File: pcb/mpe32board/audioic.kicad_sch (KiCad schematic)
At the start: 13 parts, among them J47 AudioJack3_Ground, U1 TAC5212IRGER

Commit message: layout stuff
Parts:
- C26, C27, C28, C29, C30, C31, C32, C33, C34: footprint (none) -> Capacitor_SMD:C_0603_1608Metric
- R41, R42: footprint (none) -> Resistor_SMD:R_0603_1608Metric
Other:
- note added: "https://www.ti.com/lit/ug/slau902a/slau902a.pdf (pg 11) https://github.com/t-dsp/t-dsp_tac5212_pro_audio_module/blob/main/documentation/t-dsp-tac5212-schematic.pdf"
- moved on the sheet: J47
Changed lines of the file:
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@@
 	(generator_version "9.0")
 	(paper "A4")
+	(text "https://www.ti.com/lit/ug/slau902a/slau902a.pdf (pg 11)\nhttps://github.com/t-dsp/t-dsp_tac5212_pro_audio_module/blob/main/documentation/t-dsp-tac5212-schematic.pdf"
+		(exclude_from_sim no)
+		(at 176.276 133.604 0)
+		(effects
+			(font
+				(size 1.27 1.27)
+			)
+		)
+	)
 	(junction
 		(at 119.38 57.15)
@@
 	(wire
 		(pts
-			(xy 252.73 60.96) (xy 252.73 59.69)
+			(xy 245.11 52.07) (xy 245.11 50.8)
 		)
 		(stroke
@@
 	(wire
 		(pts
-			(xy 252.73 59.69) (xy 236.22 59.69)
+			(xy 245.11 50.8) (xy 228.6 50.8)
 		)
 		(stroke
@@
 	(global_label "L_CHANNEL"
 		(shape input)
-		(at 236.22 64.77 0)
+		(at 228.6 55.88 0)
 		(fields_autoplaced yes)
 		(effects
@@
 		)
 		(property "Intersheetrefs" "${INTERSHEET_REFS}"
-			(at 249.7281 64.77 0)
+			(at 242.1081 55.88 0)
 			(effects
 				(font
@@
 	(global_label "R_CHANNEL"
 		(shape input)
-		(at 236.22 62.23 0)
+		(at 228.6 53.34 0)
 		(fields_autoplaced yes)
 		(effects
@@
 		)
 		(property "Intersheetrefs" "${INTERSHEET_REFS}"
-			(at 249.97 62.23 0)
+			(at 242.35 53.34 0)
 			(effects
 				(font
@@
 			)
 		)
-		(property "Footprint" ""
+		(property "Footprint" "Capacitor_SMD:C_0603_1608Metric"
 			(at 191.77 58.42 0)
 			(effects
@@
 			)
 		)
-		(property "Footprint" ""
+		(property "Footprint" "Capacitor_SMD:C_0603_1608Metric"
 			(at 167.64 48.26 0)
 			(effects
@@
 	(symbol
 		(lib_id "power:GND")
-		(at 231.14 69.85 0)
+		(at 223.52 60.96 0)
 		(unit 1)
 		(exclude_from_sim no)
@@
 		(fields_autoplaced yes)
 		(property "Reference" "#PWR0150"
-			(at 231.14 76.2 0)
+			(at 223.52 67.31 0)
 			(effects
 				(font
@@
 		)
 		(property "Value" "GND"
-			(at 231.14 74.93 0)
+			(at 223.52 66.04 0)
 			(effects
 				(font
@@
 		)
 		(property "Footprint" ""
-			(at 231.14 69.85 0)
+			(at 223.52 60.96 0)
 			(effects
 				(font
@@
 		)
 		(property "Datasheet" ""
-			(at 231.14 69.85 0)
+			(at 223.52 60.96 0)
 			(effects
 				(font
@@
 		)
 		(property "Description" "Power symbol creates a global label with name \"GND\" , ground"
-			(at 231.14 69.85 0)
+			(at 223.52 60.96 0)
 			(effects
 				(font
@@
 	(symbol
 		(lib_id "Connector_Audio:AudioJack3_Ground")
-		(at 231.14 62.23 0)
+		(at 223.52 53.34 0)
 		(unit 1)
 		(exclude_from_sim no)
@@
 		(fields_autoplaced yes)
 		(property "Reference" "J47"
-			(at 229.235 53.34 0)
+			(at 221.615 44.45 0)
 			(effects
 				(font
@@
 		)
 		(property "Value" "AudioJack3_Ground"
-			(at 229.235 55.88 0)
+			(at 221.615 46.99 0)
 			(effects
 				(font
@@
 		)
 		(property "Footprint" "Connector_Audio:Jack_3.5mm_CUI_SJ-3524-SMT_Horizontal"
-			(at 231.14 62.23 0)
+			(at 223.52 53.34 0)
 			(effects
 				(font
@@
 		)
 		(property "Datasheet" "~"
-			(at 231.14 62.23 0)
+			(at 223.52 53.34 0)
 			(effects
 				(font
@@
 		)
 		(property "Description" "Audio Jack, 3 Poles (Stereo / TRS), Grounded Sleeve"
-			(at 231.14 62.23 0)
+			(at 223.52 53.34 0)
 			(effects
 				(font
@@
 			)
 		)
-		(property "Footprint" ""
+		(property "Footprint" "Capacitor_SMD:C_0603_1608Metric"
 			(at 123.19 46.99 0)
 			(effects
@@
 			)
 		)
-		(property "Footprint" ""
+		(property "Footprint" "Capacitor_SMD:C_0603_1608Metric"
 			(at 143.51 57.15 0)
 			(effects
@@
 			)
 		)
-		(property "Footprint" ""
+		(property "Footprint" "Resistor_SMD:R_0603_1608Metric"
 			(at 93.98 107.95 0)
 			(effects
@@
 			)
 		)
-		(property "Footprint" ""
+		(property "Footprint" "Capacitor_SMD:C_0603_1608Metric"
 			(at 196.85 102.87 0)
 			(effects
@@
 	(symbol
 		(lib_id "power:GND")
-		(at 252.73 60.96 0)
+		(at 245.11 52.07 0)
 		(unit 1)
 		(exclude_from_sim no)
@@
 		(fields_autoplaced yes)
 		(property "Reference" "#PWR0159"
-			(at 252.73 67.31 0)
+			(at 245.11 58.42 0)
 			(effects
 				(font
@@
 		)
 		(property "Value" "GND"
-			(at 252.73 66.04 0)
+			(at 245.11 57.15 0)
 			(effects
 				(font
@@
 		)
 		(property "Footprint" ""
-			(at 252.73 60.96 0)
+			(at 245.11 52.07 0)
 			(effects
 				(font
@@
 		)
 		(property "Datasheet" ""
-			(at 252.73 60.96 0)
+			(at 245.11 52.07 0)
 			(effects
 				(font
@@
 		)
 		(property "Description" "Power symbol creates a global label with name \"GND\" , ground"
-			(at 252.73 60.96 0)
+			(at 245.11 52.07 0)
 			(effects
 				(font
@@
 			)
 		)
-		(property "Footprint" ""
+		(property "Footprint" "Capacitor_SMD:C_0603_1608Metric"
 			(at 167.64 58.42 0)
 			(effects
@@
 			)
 		)
-		(property "Footprint" ""
+		(property "Footprint" "Resistor_SMD:R_0603_1608Metric"
 			(at 93.98 100.33 0)
 			(effects
@@
 			)
 		)
-		(property "Footprint" ""
+		(property "Footprint" "Capacitor_SMD:C_0603_1608Metric"
 			(at 123.19 57.15 0)
 			(effects
@@
 			)
 		)
-		(property "Footprint" ""
+		(property "Footprint" "Capacitor_SMD:C_0603_1608Metric"
 			(at 201.93 100.33 0)
 			(effects
@@
 			)
 		)
-		(property "Footprint" ""
+		(property "Footprint" "Capacitor_SMD:C_0603_1608Metric"
 			(at 191.77 48.26 0)
 			(effects

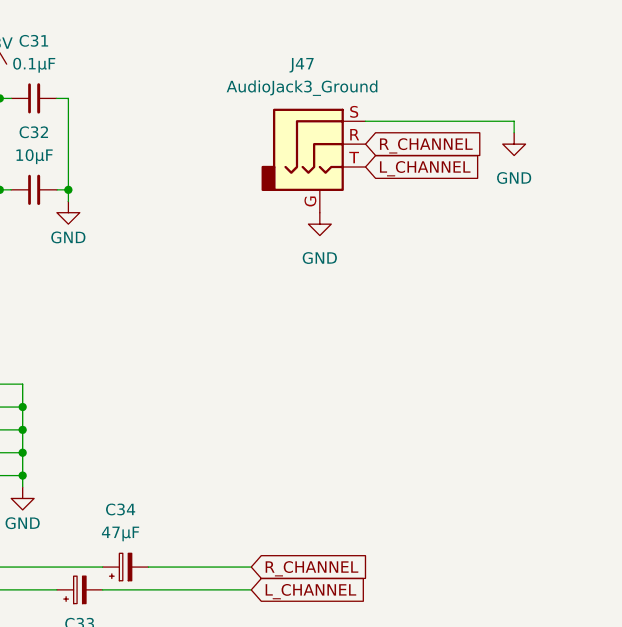
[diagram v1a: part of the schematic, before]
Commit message: routed data bus of ram
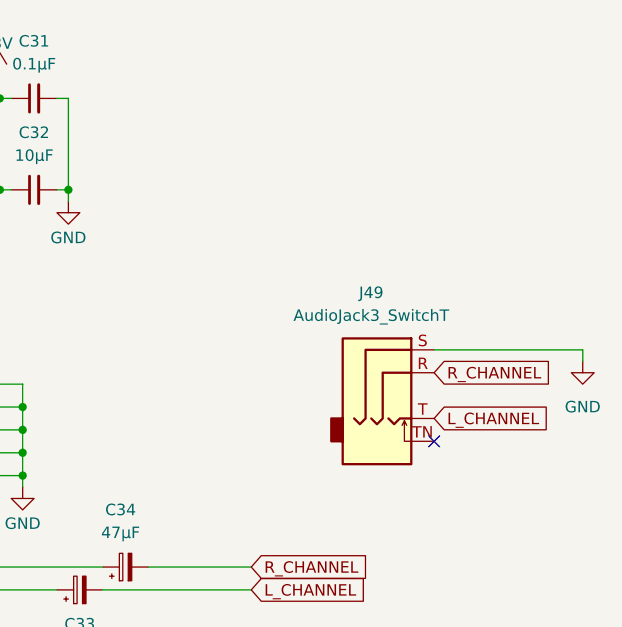
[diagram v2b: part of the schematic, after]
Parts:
- removed J47: AudioJack3_Ground, Connector_Audio:Jack_3.5mm_CUI_SJ-3524-SMT_Horizontal, symbol Connector_Audio:AudioJack3_Ground
- added J49: AudioJack3_SwitchT, Connector_Audio:Jack_3.5mm_CUI_SJ-3524-SMT_Horizontal, symbol Connector_Audio:AudioJack3_SwitchT
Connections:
- net GND: now also J49.S
- net L_CHANNEL: now also J49.T
- net R_CHANNEL: now also J49.R
- no-connect marks 5 -> 6

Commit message: routed ram
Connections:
- net I2C4_SCL renamed I2C2_SCL
- net I2C4_SDA renamed I2C2_SDA
